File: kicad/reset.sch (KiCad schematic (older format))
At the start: 15 parts

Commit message: Finished schematic.
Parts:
- gave numbers to parts that had none: 11
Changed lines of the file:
@@
 	4550 2975 5550 2975
 $Comp
-L Device:R R?
+L Device:R R38
 U 1 1 5E32EF8D
 P 6400 3325
-F 0 "R?" H 6470 3371 50  0000 L CNN
+F 0 "R38" H 6470 3371 50  0000 L CNN
 F 1 "100K" H 6470 3280 50  0000 L CNN
 F 2 "" V 6330 3325 50  0001 C CNN
@@
 $EndComp
 $Comp
-L Device:C C?
+L Device:C C16
 U 1 1 5E32FF59
 P 6400 3825
-F 0 "C?" H 6515 3871 50  0000 L CNN
+F 0 "C16" H 6515 3871 50  0000 L CNN
 F 1 "100nF" H 6515 3780 50  0000 L CNN
 F 2 "" H 6438 3675 50  0001 C CNN
@@
 	6400 3575 6400 3675
 $Comp
-L Device:R R?
+L Device:R R35
 U 1 1 5E3316E5
 P 3200 3325
-F 0 "R?" H 3270 3371 50  0000 L CNN
+F 0 "R35" H 3270 3371 50  0000 L CNN
 F 1 "100K" H 3270 3280 50  0000 L CNN
 F 2 "" V 3130 3325 50  0001 C CNN
@@
 $EndComp
 $Comp
-L Device:C C?
+L Device:C C15
 U 1 1 5E3316EF
 P 3200 3825
-F 0 "C?" H 3315 3871 50  0000 L CNN
+F 0 "C15" H 3315 3871 50  0000 L CNN
 F 1 "100nF" H 3315 3780 50  0000 L CNN
 F 2 "" H 3238 3675 50  0001 C CNN
@@
 	2225 2975 2500 2975
 $Comp
-L power:VCC #PWR?
+L power:VCC #PWR036
 U 1 1 5E3377D4
 P 2225 2975
-F 0 "#PWR?" H 2225 2825 50  0001 C CNN
+F 0 "#PWR036" H 2225 2825 50  0001 C CNN
 F 1 "VCC" H 2242 3148 50  0000 C CNN
 F 2 "" H 2225 2975 50  0001 C CNN
@@
 Connection ~ 2225 2975
 $Comp
-L Device:C C?
+L Device:C C14
 U 1 1 5E337F5C
 P 1875 2975
-F 0 "C?" V 2127 2975 50  0000 C CNN
+F 0 "C14" V 2127 2975 50  0000 C CNN
 F 1 "100nF" V 2036 2975 50  0000 C CNN
 F 2 "" H 1913 2825 50  0001 C CNN
@@
 $EndComp
 $Comp
-L power:GND #PWR?
+L power:GND #PWR037
 U 1 1 5E339564
 P 4025 4325
-F 0 "#PWR?" H 4025 4075 50  0001 C CNN
+F 0 "#PWR037" H 4025 4075 50  0001 C CNN
 F 1 "GND" H 4030 4152 50  0000 C CNN
 F 2 "" H 4025 4325 50  0001 C CNN
@@
 	9350 2975 9825 2975
 $Comp
-L Switch:SW_Push SW?
+L Switch:SW_Push SW1
 U 1 1 5E354331
 P 2950 1550
-F 0 "SW?" H 2950 1835 50  0000 C CNN
+F 0 "SW1" H 2950 1835 50  0000 C CNN
 F 1 "RESET/RESTART" H 2950 1744 50  0000 C CNN
 F 2 "" H 2950 1750 50  0001 C CNN
@@
 	2500 2975 3200 2975
 $Comp
-L Transistor_BJT:PN2222A Q?
+L Transistor_BJT:PN2222A Q1
 U 1 1 5E3565A7
 P 3775 2425
-F 0 "Q?" H 3966 2379 50  0000 L CNN
+F 0 "Q1" H 3966 2379 50  0000 L CNN
 F 1 "PN2222A" H 3966 2470 50  0000 L CNN
 F 2 "Package_TO_SOT_THT:TO-92_Inline" H 3975 2350 50  0001 L CIN
@@
 $EndComp
 $Comp
-L Transistor_BJT:PN2222A Q?
+L Transistor_BJT:PN2222A Q2
 U 1 1 5E358341
 P 6975 2400
-F 0 "Q?" H 7166 2354 50  0000 L CNN
+F 0 "Q2" H 7166 2354 50  0000 L CNN
 F 1 "PN2222A" H 7166 2445 50  0000 L CNN
 F 2 "Package_TO_SOT_THT:TO-92_Inline" H 7175 2325 50  0001 L CIN
@@
 Connection ~ 6875 2975
 $Comp
-L power:GND #PWR?
+L power:GND #PWR038
 U 1 1 5E361C8A
 P 6175 2000
-F 0 "#PWR?" H 6175 1750 50  0001 C CNN
+F 0 "#PWR038" H 6175 1750 50  0001 C CNN
 F 1 "GND" H 6180 1827 50  0000 C CNN
 F 2 "" H 6175 2000 50  0001 C CNN
@@
 $EndComp
 $Comp
-L Device:R R?
+L Device:R R36
 U 1 1 5E368EE7
 P 3675 1775
-F 0 "R?" H 3745 1821 50  0000 L CNN
+F 0 "R36" H 3745 1821 50  0000 L CNN
 F 1 "100K" H 3745 1730 50  0000 L CNN
 F 2 "" V 3605 1775 50  0001 C CNN
@@
 	3675 2000 6175 2000
 $Comp
-L Device:R R?
+L Device:R R37
 U 1 1 5E371EB3
 P 4700 1550
-F 0 "R?" V 4493 1550 50  0000 C CNN
+F 0 "R37" V 4493 1550 50  0000 C CNN
 F 1 "1K" V 4584 1550 50  0000 C CNN
 F 2 "" V 4630 1550 50  0001 C CNN
@@
 	2025 2975 2225 2975
 $Comp
-L Local:74HC14 U?
+L Local:74HC14 U4
 U 1 1 5F057356
 P 4250 2975
-F 0 "U?" H 4250 3292 50  0000 C CNN
+F 0 "U4" H 4250 3292 50  0000 C CNN
 F 1 "74HC14" H 4250 3201 50  0000 C CNN
 F 2 "" H 4250 2975 50  0001 C CNN
@@
 $EndComp
 $Comp
-L Local:74HC14 U?
+L Local:74HC14 U4
 U 2 1 5F05BC8E
 P 5850 2975
-F 0 "U?" H 5850 3292 50  0000 C CNN
+F 0 "U4" H 5850 3292 50  0000 C CNN
 F 1 "74HC14" H 5850 3201 50  0000 C CNN
 F 2 "" H 5850 2975 50  0001 C CNN
@@
 $EndComp
 $Comp
-L Local:74HC14 U?
+L Local:74HC14 U4
 U 3 1 5F05CC54
 P 7450 2975
-F 0 "U?" H 7450 3292 50  0000 C CNN
+F 0 "U4" H 7450 3292 50  0000 C CNN
 F 1 "74HC14" H 7450 3201 50  0000 C CNN
 F 2 "" H 7450 2975 50  0001 C CNN
@@
 $EndComp
 $Comp
-L Local:74HC14 U?
+L Local:74HC14 U4
 U 4 1 5F05DA22
 P 9050 2975
-F 0 "U?" H 9050 3292 50  0000 C CNN
+F 0 "U4" H 9050 3292 50  0000 C CNN
 F 1 "74HC14" H 9050 3201 50  0000 C CNN
 F 2 "" H 9050 2975 50  0001 C CNN
@@
 $EndComp
 $Comp
-L Local:74HC14 U?
+L Local:74HC14 U4
 U 7 1 5F05EEBF
 P 2225 3675
-F 0 "U?" H 2455 3721 50  0000 L CNN
+F 0 "U4" H 2455 3721 50  0000 L CNN
 F 1 "74HC14" H 2455 3630 50  0000 L CNN
 F 2 "" H 2225 3675 50  0001 C CNN

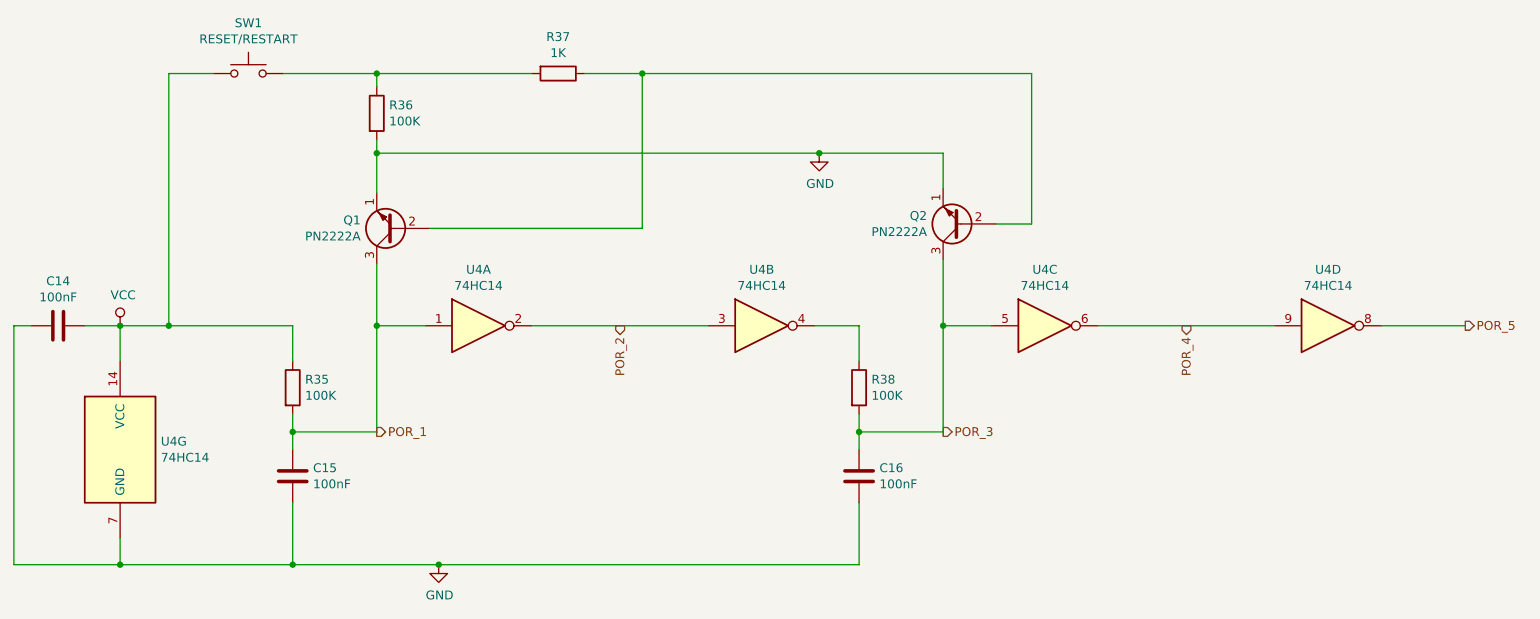
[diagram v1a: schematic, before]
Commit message: KiCad: Added missing inverter on comparator output.
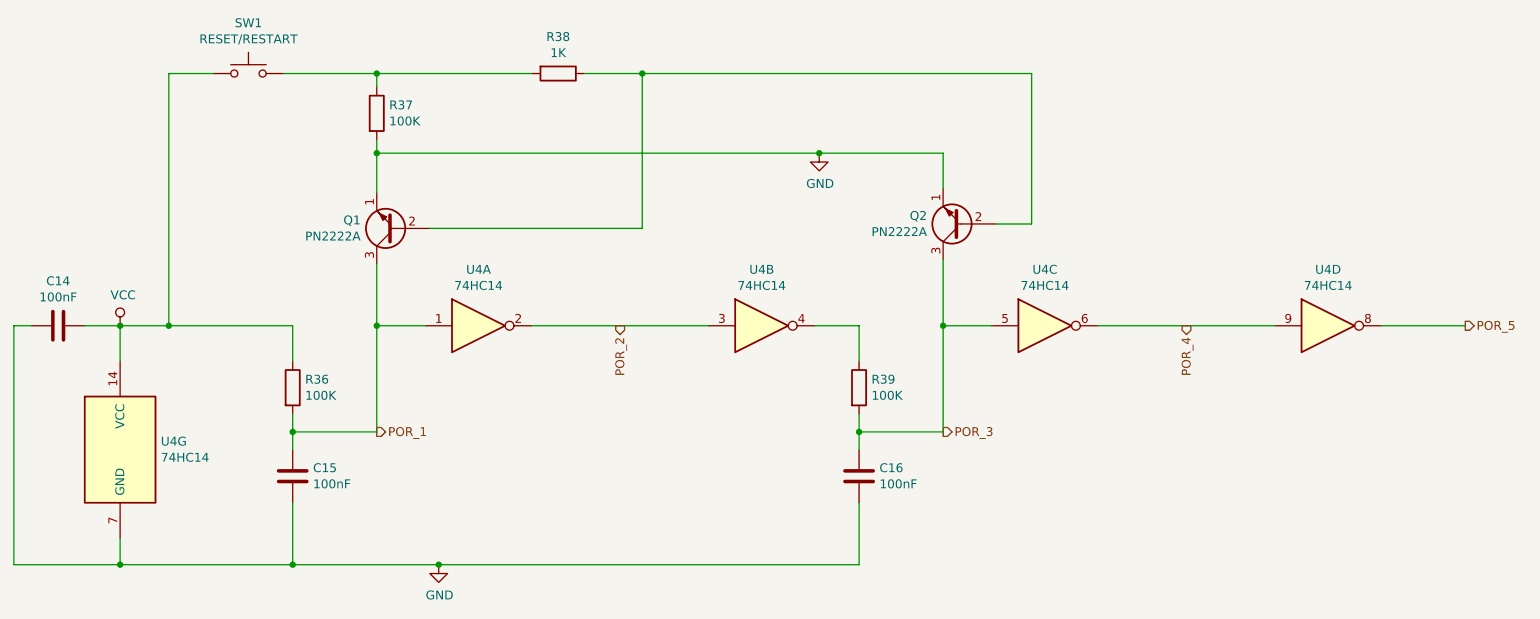
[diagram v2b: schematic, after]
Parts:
- renumbered R35 to R36, R36 to R37, R37 to R38, R38 to R39
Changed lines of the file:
@@
 	4550 2975 5550 2975
 $Comp
-L Device:R R38
+L Device:R R39
 U 1 1 5E32EF8D
 P 6400 3325
-F 0 "R38" H 6470 3371 50  0000 L CNN
+F 0 "R39" H 6470 3371 50  0000 L CNN
 F 1 "100K" H 6470 3280 50  0000 L CNN
 F 2 "" V 6330 3325 50  0001 C CNN
@@
 	6400 3575 6400 3675
 $Comp
-L Device:R R35
+L Device:R R36
 U 1 1 5E3316E5
 P 3200 3325
-F 0 "R35" H 3270 3371 50  0000 L CNN
+F 0 "R36" H 3270 3371 50  0000 L CNN
 F 1 "100K" H 3270 3280 50  0000 L CNN
 F 2 "" V 3130 3325 50  0001 C CNN
@@
 	2225 2975 2500 2975
 $Comp
-L power:VCC #PWR036
+L power:VCC #PWR037
 U 1 1 5E3377D4
 P 2225 2975
-F 0 "#PWR036" H 2225 2825 50  0001 C CNN
+F 0 "#PWR037" H 2225 2825 50  0001 C CNN
 F 1 "VCC" H 2242 3148 50  0000 C CNN
 F 2 "" H 2225 2975 50  0001 C CNN
@@
 $EndComp
 $Comp
-L power:GND #PWR037
+L power:GND #PWR038
 U 1 1 5E339564
 P 4025 4325
-F 0 "#PWR037" H 4025 4075 50  0001 C CNN
+F 0 "#PWR038" H 4025 4075 50  0001 C CNN
 F 1 "GND" H 4030 4152 50  0000 C CNN
 F 2 "" H 4025 4325 50  0001 C CNN
@@
 Connection ~ 6875 2975
 $Comp
-L power:GND #PWR038
+L power:GND #PWR039
 U 1 1 5E361C8A
 P 6175 2000
-F 0 "#PWR038" H 6175 1750 50  0001 C CNN
+F 0 "#PWR039" H 6175 1750 50  0001 C CNN
 F 1 "GND" H 6180 1827 50  0000 C CNN
 F 2 "" H 6175 2000 50  0001 C CNN
@@
 $EndComp
 $Comp
-L Device:R R36
+L Device:R R37
 U 1 1 5E368EE7
 P 3675 1775
-F 0 "R36" H 3745 1821 50  0000 L CNN
+F 0 "R37" H 3745 1821 50  0000 L CNN
 F 1 "100K" H 3745 1730 50  0000 L CNN
 F 2 "" V 3605 1775 50  0001 C CNN
@@
 	3675 2000 6175 2000
 $Comp
-L Device:R R37
+L Device:R R38
 U 1 1 5E371EB3
 P 4700 1550
-F 0 "R37" V 4493 1550 50  0000 C CNN
+F 0 "R38" V 4493 1550 50  0000 C CNN
 F 1 "1K" V 4584 1550 50  0000 C CNN
 F 2 "" V 4630 1550 50  0001 C CNN

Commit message: KiCad: Added opcode to enable/disable input and 64 respawn checkpoints.
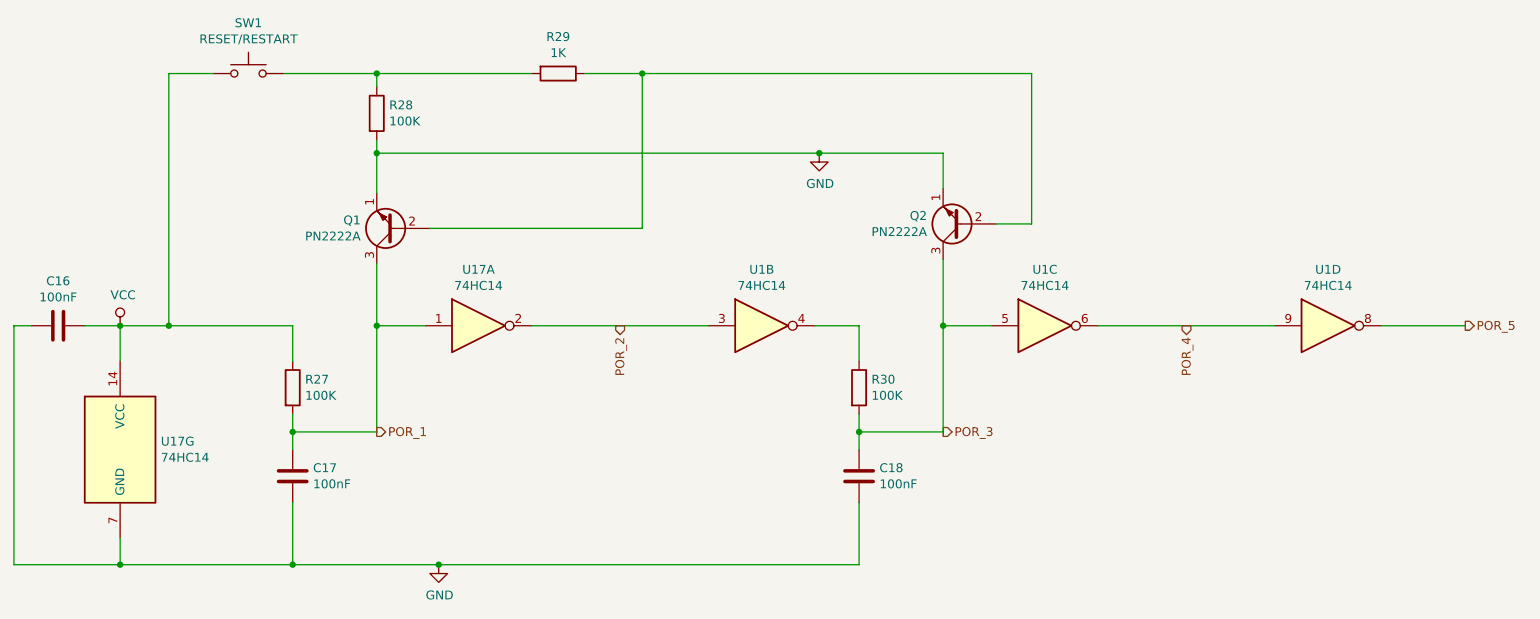
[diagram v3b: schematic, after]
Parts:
- renumbered C14 to C16, C15 to C17, C16 to C18, R36 to R27, R37 to R28, R38 to R29, R39 to R30, U4 to U1, U4 to U17
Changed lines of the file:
@@
 $Descr A4 11693 8268
 encoding utf-8
-Sheet 3 4
+Sheet 3 5
 Title "Power on Reset Circuit"
 Date "2019-09-12"
@@
 	4550 2975 5550 2975
 $Comp
-L Device:R R39
+L Device:R R30
 U 1 1 5E32EF8D
 P 6400 3325
-F 0 "R39" H 6470 3371 50  0000 L CNN
+F 0 "R30" H 6470 3371 50  0000 L CNN
 F 1 "100K" H 6470 3280 50  0000 L CNN
 F 2 "" V 6330 3325 50  0001 C CNN
@@
 $EndComp
 $Comp
-L Device:C C16
+L Device:C C18
 U 1 1 5E32FF59
 P 6400 3825
-F 0 "C16" H 6515 3871 50  0000 L CNN
+F 0 "C18" H 6515 3871 50  0000 L CNN
 F 1 "100nF" H 6515 3780 50  0000 L CNN
 F 2 "" H 6438 3675 50  0001 C CNN
@@
 	6400 3575 6400 3675
 $Comp
-L Device:R R36
+L Device:R R27
 U 1 1 5E3316E5
 P 3200 3325
-F 0 "R36" H 3270 3371 50  0000 L CNN
+F 0 "R27" H 3270 3371 50  0000 L CNN
 F 1 "100K" H 3270 3280 50  0000 L CNN
 F 2 "" V 3130 3325 50  0001 C CNN
@@
 $EndComp
 $Comp
-L Device:C C15
+L Device:C C17
 U 1 1 5E3316EF
 P 3200 3825
-F 0 "C15" H 3315 3871 50  0000 L CNN
+F 0 "C17" H 3315 3871 50  0000 L CNN
 F 1 "100nF" H 3315 3780 50  0000 L CNN
 F 2 "" H 3238 3675 50  0001 C CNN
@@
 	2225 2975 2500 2975
 $Comp
-L power:VCC #PWR037
+L power:VCC #PWR040
 U 1 1 5E3377D4
 P 2225 2975
-F 0 "#PWR037" H 2225 2825 50  0001 C CNN
+F 0 "#PWR040" H 2225 2825 50  0001 C CNN
 F 1 "VCC" H 2242 3148 50  0000 C CNN
 F 2 "" H 2225 2975 50  0001 C CNN
@@
 Connection ~ 2225 2975
 $Comp
-L Device:C C14
+L Device:C C16
 U 1 1 5E337F5C
 P 1875 2975
-F 0 "C14" V 2127 2975 50  0000 C CNN
+F 0 "C16" V 2127 2975 50  0000 C CNN
 F 1 "100nF" V 2036 2975 50  0000 C CNN
 F 2 "" H 1913 2825 50  0001 C CNN
@@
 $EndComp
 $Comp
-L power:GND #PWR038
+L power:GND #PWR041
 U 1 1 5E339564
 P 4025 4325
-F 0 "#PWR038" H 4025 4075 50  0001 C CNN
+F 0 "#PWR041" H 4025 4075 50  0001 C CNN
 F 1 "GND" H 4030 4152 50  0000 C CNN
 F 2 "" H 4025 4325 50  0001 C CNN
@@
 Connection ~ 6875 2975
 $Comp
-L power:GND #PWR039
+L power:GND #PWR042
 U 1 1 5E361C8A
 P 6175 2000
-F 0 "#PWR039" H 6175 1750 50  0001 C CNN
+F 0 "#PWR042" H 6175 1750 50  0001 C CNN
 F 1 "GND" H 6180 1827 50  0000 C CNN
 F 2 "" H 6175 2000 50  0001 C CNN
@@
 $EndComp
 $Comp
-L Device:R R37
+L Device:R R28
 U 1 1 5E368EE7
 P 3675 1775
-F 0 "R37" H 3745 1821 50  0000 L CNN
+F 0 "R28" H 3745 1821 50  0000 L CNN
 F 1 "100K" H 3745 1730 50  0000 L CNN
 F 2 "" V 3605 1775 50  0001 C CNN
@@
 	3675 2000 6175 2000
 $Comp
-L Device:R R38
+L Device:R R29
 U 1 1 5E371EB3
 P 4700 1550
-F 0 "R38" V 4493 1550 50  0000 C CNN
+F 0 "R29" V 4493 1550 50  0000 C CNN
 F 1 "1K" V 4584 1550 50  0000 C CNN
 F 2 "" V 4630 1550 50  0001 C CNN
@@
 	2025 2975 2225 2975
 $Comp
-L Local:74HC14 U4
+L Local:74HC14 U17
 U 1 1 5F057356
 P 4250 2975
-F 0 "U4" H 4250 3292 50  0000 C CNN
+F 0 "U17" H 4250 3292 50  0000 C CNN
 F 1 "74HC14" H 4250 3201 50  0000 C CNN
 F 2 "" H 4250 2975 50  0001 C CNN
@@
 $EndComp
 $Comp
-L Local:74HC14 U4
+L Local:74HC14 U1
 U 2 1 5F05BC8E
 P 5850 2975
-F 0 "U4" H 5850 3292 50  0000 C CNN
+F 0 "U1" H 5850 3292 50  0000 C CNN
 F 1 "74HC14" H 5850 3201 50  0000 C CNN
 F 2 "" H 5850 2975 50  0001 C CNN
@@
 $EndComp
 $Comp
-L Local:74HC14 U4
+L Local:74HC14 U1
 U 3 1 5F05CC54
 P 7450 2975
-F 0 "U4" H 7450 3292 50  0000 C CNN
+F 0 "U1" H 7450 3292 50  0000 C CNN
 F 1 "74HC14" H 7450 3201 50  0000 C CNN
 F 2 "" H 7450 2975 50  0001 C CNN
@@
 $EndComp
 $Comp
-L Local:74HC14 U4
+L Local:74HC14 U1
 U 4 1 5F05DA22
 P 9050 2975
-F 0 "U4" H 9050 3292 50  0000 C CNN
+F 0 "U1" H 9050 3292 50  0000 C CNN
 F 1 "74HC14" H 9050 3201 50  0000 C CNN
 F 2 "" H 9050 2975 50  0001 C CNN
@@
 $EndComp
 $Comp
-L Local:74HC14 U4
+L Local:74HC14 U17
 U 7 1 5F05EEBF
 P 2225 3675
-F 0 "U4" H 2455 3721 50  0000 L CNN
+F 0 "U17" H 2455 3721 50  0000 L CNN
 F 1 "74HC14" H 2455 3630 50  0000 L CNN
 F 2 "" H 2225 3675 50  0001 C CNN
